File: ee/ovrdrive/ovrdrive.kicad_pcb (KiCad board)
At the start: 4 copper layers, 37.2 x 15 mm, 47 parts, among them J1 USB_A, Q1 Q_NMOS_DGS, U1 SM3257ENT, U2 FLASH, U3 ATtiny24A-MM, U4 74AUC1G32, U5 LMV321, U6 LM4040DBZ-2.5

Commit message: R0.1 released
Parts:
- JP1: moved to B.Cu
- moved JP1 4.10 mm to (129.4, 109.0), turned to 0 degrees
- moved JP2 1.91 mm to (138.1, 110.2)
- moved D2 0.10 mm to (139.6, 100.3)
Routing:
- net Net-(JP1-Pad2): track 5.93 -> 2.37 mm, vias 0 -> 1
- net +3.3V: track 40.1 -> 42.8 mm
- net Net-(JP2-Pad2): track 6.72 -> 8.53 mm
- net GND: vias 2 -> 13
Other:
- board text added: "OVRDRIVE Ryan Walker Interrupt Labs R0.1"

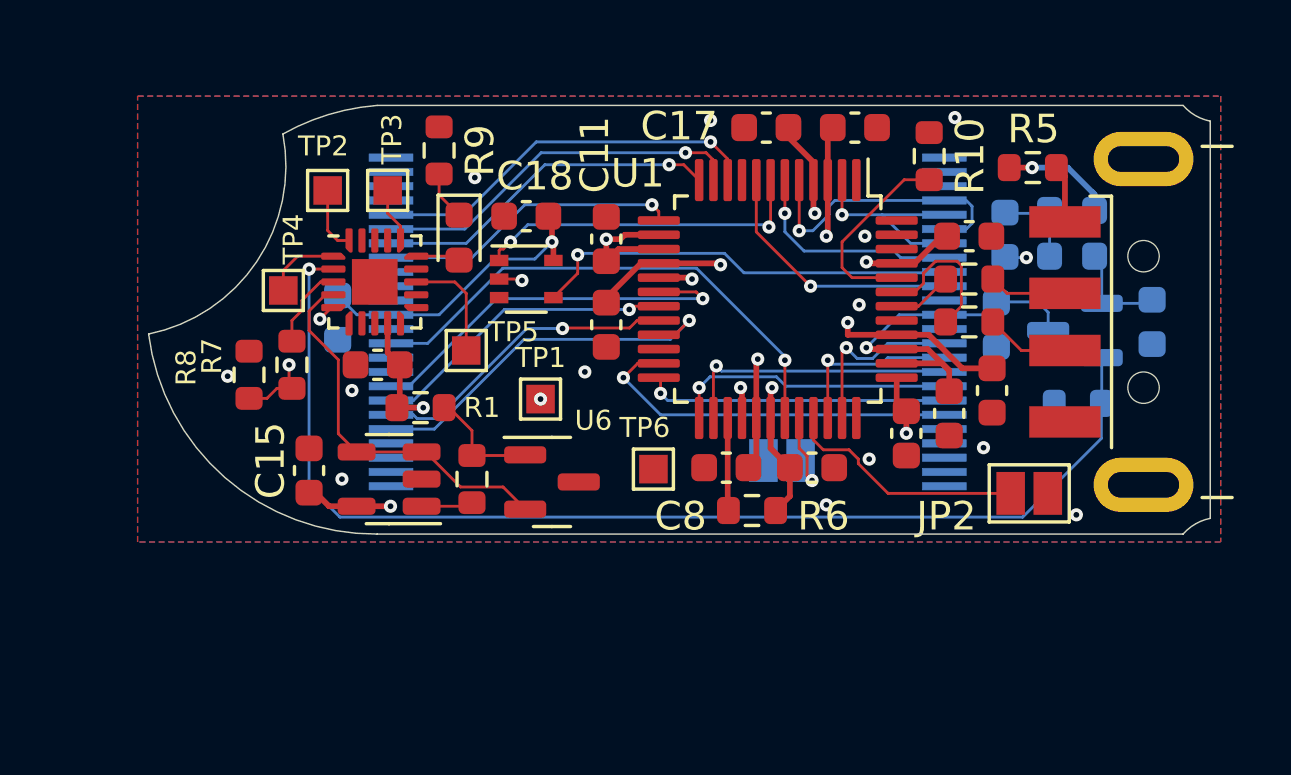
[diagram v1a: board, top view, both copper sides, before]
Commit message: Removed analog circuitry for spit detection, shortened entire board by 0.6mm to fit in enclosure.
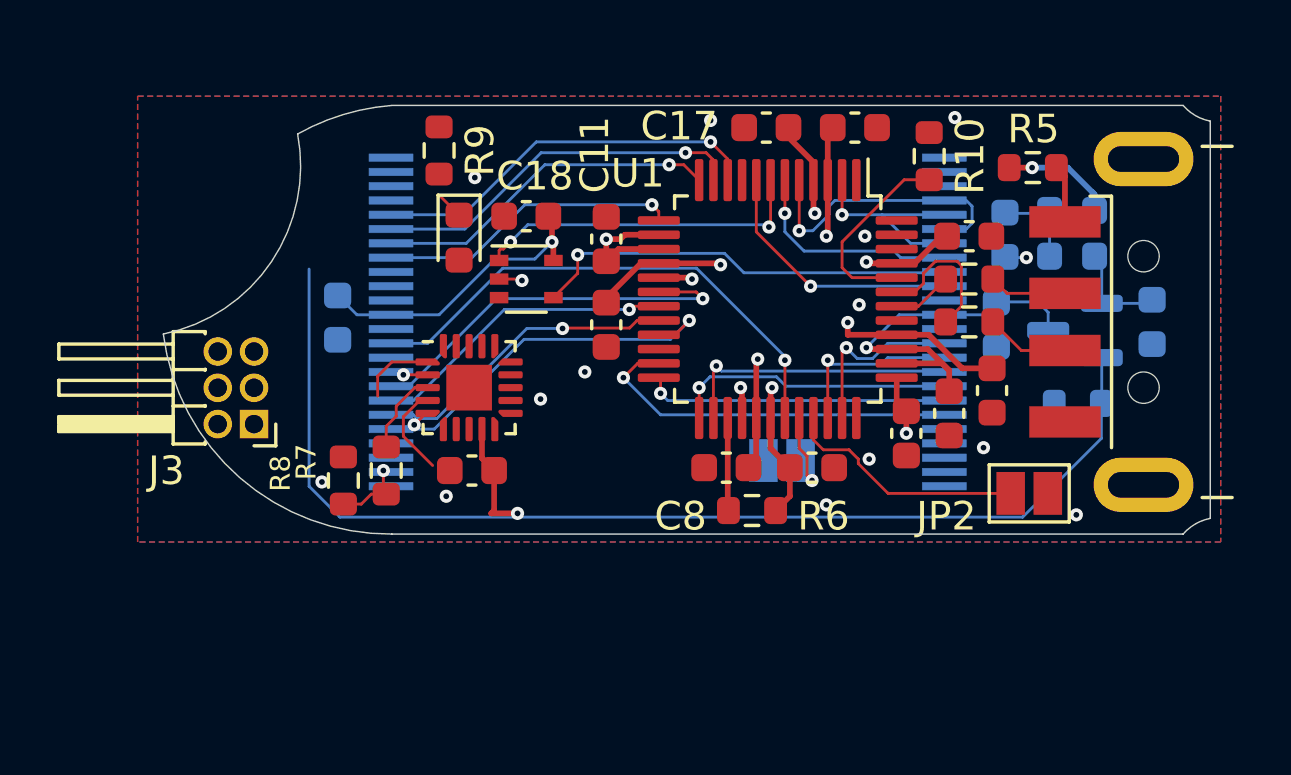
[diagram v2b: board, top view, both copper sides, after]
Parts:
- removed C15: 100nF, Capacitor_SMD:C_0603_1608Metric
- removed R1: 10k, Resistor_SMD:R_0603_1608Metric
- removed R2: 747k, Resistor_SMD:R_0603_1608Metric
- removed TP1, TP2, TP3, TP4, TP5, TP6: TestPoint, TestPoint:TestPoint_Pad_1.0x1.0mm
- removed U5: LMV321, Package_TO_SOT_SMD:SOT-23-5
- removed U6: LM4040DBZ-2.5, Package_TO_SOT_SMD:SOT-23
- added J3: Conn_02x03_Counter_Clockwise, Connector_PinHeader_1.27mm:PinHeader_2x03_P1.27mm_Horizontal, F.Cu at (111.0, 107.8)
- Q1: value Q_NMOS_DGS -> RU1J002YNTCL
- moved C4 4.96 mm to (118.6, 109.4)
- moved R7 4.96 mm to (115.6, 109.4)
- moved R8 4.96 mm to (114.1, 109.8)
- moved U3 4.96 mm to (118.5, 106.5)
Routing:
- net /Vs: track 13.4 -> 3.22 mm
- net Net-(R1-Pad2): track 4.05 -> 0.00 mm
- net /~{RST}: track 3.92 -> 0.00 mm
- net +5V: track 47.8 -> 44.7 mm, vias 5 -> 4
- net /MISO: track 2.29 -> 0.00 mm
- net /MOSI: track 1.94 -> 0.00 mm
- net Net-(J2-Pad2): track 1.81 -> 0.00 mm
- net Net-(D1-Pad2): track 1.56 -> 0.19 mm
- net Net-(D1-Pad1): track 1.73 -> 0.99 mm
- net GND: vias 13 -> 12
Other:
- board size 37.2 x 15 mm -> 36.6 x 15 mm

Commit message: Changes components and a leftover commit.
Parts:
- added C15: 22uF, Capacitor_SMD:C_0603_1608Metric, B.Cu at (139.6, 103.4)
- added D4: D_Schottky, Diode_SMD:D_0603_1608Metric, B.Cu at (113.9, 101.0)
- added Q2: SSM3J328R,LF, Package_TO_SOT_SMD:SOT-23, B.Cu at (139.3, 107.6)
- added Q3: RU1J002YNTCL, Package_TO_SOT_SMD:SOT-523, B.Cu at (142.5, 104.2)
- added R1: 1k, Resistor_SMD:R_0402_1005Metric, F.Cu at (115.1, 102.4)
- added R12: 1k, Resistor_SMD:R_0402_1005Metric, F.Cu at (123.1, 109.5)
- added R13: 1R, Resistor_SMD:R_0603_1608Metric, F.Cu at (116.9, 110.0)
- added R2: 10k, Resistor_SMD:R_0402_1005Metric, F.Cu at (114.8, 109.3)
- added TH1: 10k, Resistor_SMD:R_0603_1608Metric, F.Cu at (116.9, 108.5)
- added TP1: TestPoint, TestPoint:TestPoint_Pad_D1.0mm, F.Cu at (121.0, 105.7)
- added TP2: TestPoint, TestPoint:TestPoint_Pad_D1.0mm, F.Cu at (121.7, 103.1)
- C14: value 100nF -> 22uF
- D2, D3: value D -> D_Schottky
- Q1: value RU1J002YNTCL -> SSM3J328R,LF; moved to F.Cu
- R11: value 2.2R -> 1k; footprint Resistor_SMD:R_0603_1608Metric -> Resistor_SMD:R_0402_1005Metric
- R7, R8, R9: footprint Resistor_SMD:R_0603_1608Metric -> Resistor_SMD:R_0402_1005Metric
- moved Q1 19.8 mm to (120.6, 109.5)
- moved R8 5.35 mm to (113.9, 104.4)
- moved R7 5.05 mm to (114.9, 104.4)
- moved D1 2.93 mm to (117.5, 98.4)
- moved C14 2.89 mm to (139.6, 104.9), turned to 180 degrees
- moved C18 2.89 mm to (119.8, 97.7)
- moved U4 2.89 mm to (119.8, 99.9)
- moved C4 2.69 mm to (117.9, 106.8)
- moved U3 2.69 mm to (117.8, 103.9)
- moved R11 2.49 mm to (142.1, 108.0), turned to 180 degrees
- moved R9 1.56 mm to (115.9, 98.4), turned to 90 degrees
- moved J3 1.10 mm to (112.1, 107.8)
- turned C1 to 90 degrees
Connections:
- C1 pad 1: +3.3V -> Net-(D4-K)
- C14 pad 1: Net-(C14-Pad1) -> Net-(D3-K)
- C2 pad 1: +3.3V -> Net-(D4-K)
- D3 pad 1: Net-(C14-Pad1) -> Net-(D3-K)
- J3 pad 1: /MISO -> +5V
- J3 pad 6: +5V -> /MISO
- Q1 pad 1: Net-(C14-Pad1) -> /PB2
- Q1 pad 2: /KILL -> +5V
- Q1 pad 3: +3.3V -> Net-(Q1-D)
- R11 pad 1: GND -> Net-(Q2-G)
- R11 pad 2: /KILL -> Net-(D3-K)
- U2 pad 12: +3.3V -> Net-(D4-K)
- U2 pad 37: +3.3V -> Net-(D4-K)
- U3 pad 11: unconnected-(U3-Pad11) -> /PB0
- U3 pad 12: unconnected-(U3-Pad12) -> /PB1
- U3 pad 14: unconnected-(U3-Pad14) -> /PB2
- U3 pad 4: /Vs -> /PA1
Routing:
- net Net-(D4-K): track 0.00 -> 24.9 mm
- net /Distruct_PWM: track 41.3 -> 25.2 mm
- net /PB2: track 0.00 -> 15.0 mm, vias 0 -> 2
- net /~{RST}: track 0.00 -> 14.8 mm, vias 0 -> 1
- net /MOSI: track 0.00 -> 13.0 mm, vias 0 -> 1
- net /MISO: track 0.00 -> 8.84 mm
- net Net-(Q2-G): track 0.00 -> 8.58 mm
- net /PA1: track 0.00 -> 6.06 mm
- net +5V: track 44.7 -> 39.3 mm
- net Net-(D1-A): track 0.19 -> 5.34 mm
- net /SCK: track 2.66 -> 6.79 mm
- net +3.3V: track 42.8 -> 38.9 mm
- net /INHIBIT: track 13.8 -> 10.1 mm
- net Net-(C14-Pad1): track 3.57 -> 0.00 mm
- net /KILL: track 40.6 -> 37.2 mm, vias 1 -> 2
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- added copper zone on F.Cu, net +5V
- added copper zone on B.Cu, net Net-(D3-K)
- added copper zone on B.Cu, net Net-(D4-K)
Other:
- board text added: "OVRDRIVE Interrupt Labs R0.2"
- board text removed: "OVRDRIVE Ryan Walker Interrupt Labs R0.1"

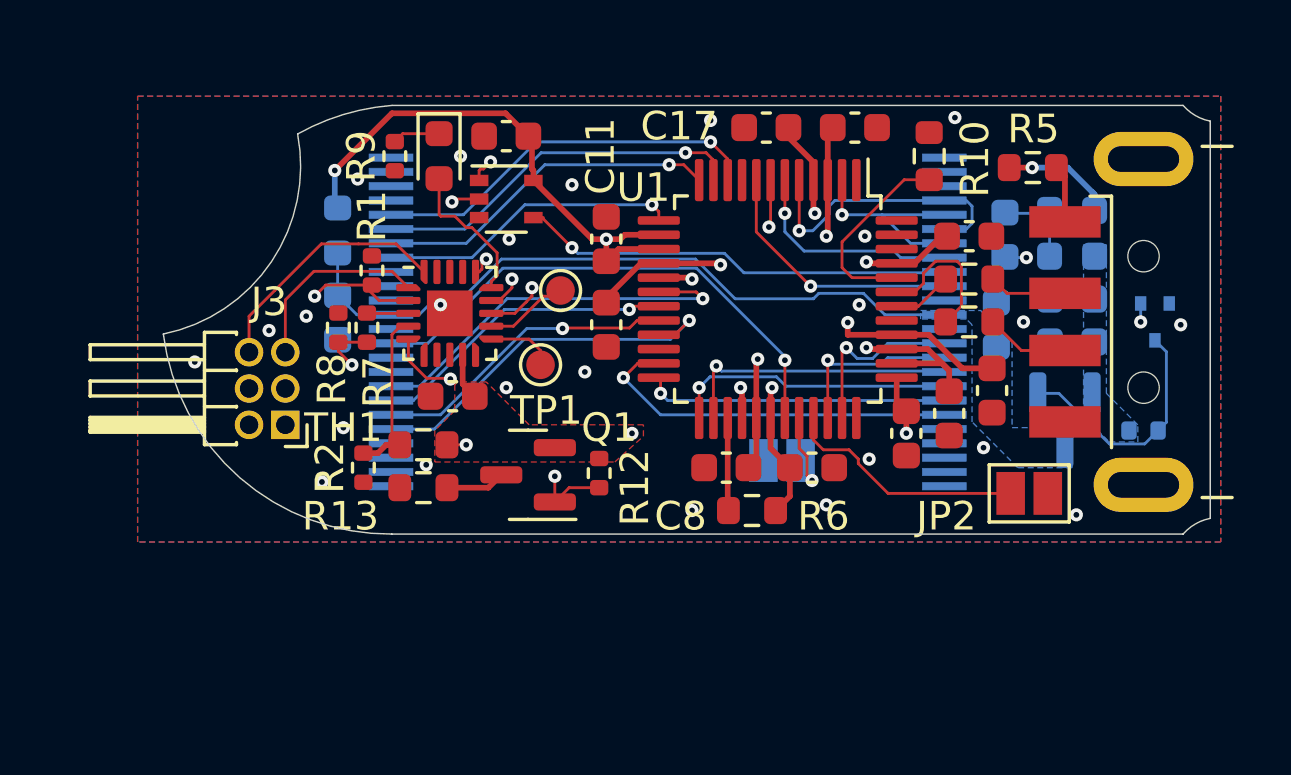
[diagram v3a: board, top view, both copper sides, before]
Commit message: Change the destruction circuit to an H-bridge.
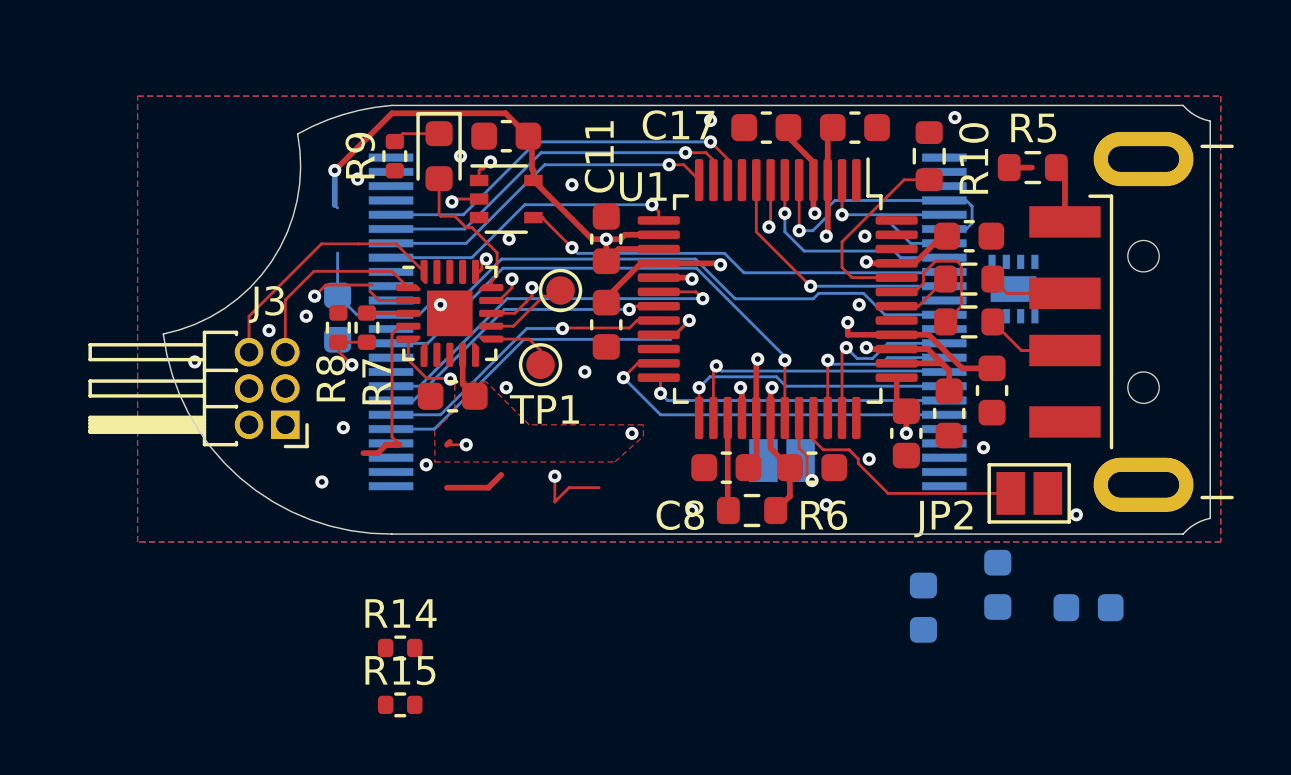
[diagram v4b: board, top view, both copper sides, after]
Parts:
- removed C15: 22uF, Capacitor_SMD:C_0603_1608Metric
- removed D2, D3, D4: D_Schottky, Diode_SMD:D_0603_1608Metric
- removed Q1, Q2: SSM3J328R,LF, Package_TO_SOT_SMD:SOT-23
- removed Q3: RU1J002YNTCL, Package_TO_SOT_SMD:SOT-523
- removed R1, R11, R12: 1k, Resistor_SMD:R_0402_1005Metric
- removed R13: 1R, Resistor_SMD:R_0603_1608Metric
- removed R2: 10k, Resistor_SMD:R_0402_1005Metric
- removed TH1: 10k, Resistor_SMD:R_0603_1608Metric
- added R14: 10k, Resistor_SMD:R_0402_1005Metric, F.Cu at (116.1, 115.6)
- added R15: 10k, Resistor_SMD:R_0402_1005Metric, F.Cu at (116.1, 117.6)
- added U5: DRV8837C, Package_SON:WSON-8-1EP_2x2mm_P0.5mm_EP0.9x1.6mm, B.Cu at (137.6, 103.0)
- C14: value 22uF -> 1uF
- C3: value 100nF -> 1uF
- U4: value 74AUC1G32 -> SN74LVC1G32DCKR
- moved C3 13.4 mm to (134.4, 114.2)
- moved C14 9.32 mm to (140.2, 114.2)
- moved C1 9.10 mm to (137.0, 113.4)
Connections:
- net Net-(D4-K) renamed VMEM
- C1 pad 2: GND -> VS
- C18 pad 2: GND -> VS
- C2 pad 2: GND -> VS
- C3 pad 2: /Distruct_PWM -> GND
- TP1 pad 1: /PB0 -> /PB1
- TP2 pad 1: /PB1 -> /PB2
- U2 pad 13: GND -> VS
- U2 pad 36: GND -> VS
- U3 pad 11: /PB0 -> /CHG2
- U3 pad 2: /KILL -> /CHG1
- U3 pad 4: /PA1 -> /IN2
- U3 pad 5: /Distruct_PWM -> /IN1
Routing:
- net /KILL: track 37.2 -> 0.00 mm, vias 2 -> 0
- net (no net): track 0.00 -> 37.2 mm, vias 0 -> 1
- net /Distruct_PWM: track 25.2 -> 0.00 mm, vias 2 -> 0
- net /IN1: track 0.00 -> 24.5 mm, vias 0 -> 1
- net Net-(Q2-G): track 8.58 -> 0.00 mm
- net /PA1: track 6.06 -> 0.00 mm
- net /IN2: track 0.00 -> 6.06 mm
- net +5V: track 39.3 -> 36.1 mm, vias 4 -> 3
- net Net-(D2-K): track 3.04 -> 0.00 mm
- net /PB1: track 2.94 -> 5.33 mm
- net /PB0: track 2.39 -> 0.00 mm
- net Net-(Q1-D): track 2.09 -> 0.00 mm
- net /CHG1: track 0.00 -> 1.48 mm
- net GND: track 0.04 -> 0.00 mm, vias 24 -> 22
- removed copper zone on B.Cu, net Net-(D3-K)
- removed copper zone on B.Cu, net VMEM

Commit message: Started the routing the new H-bridge.
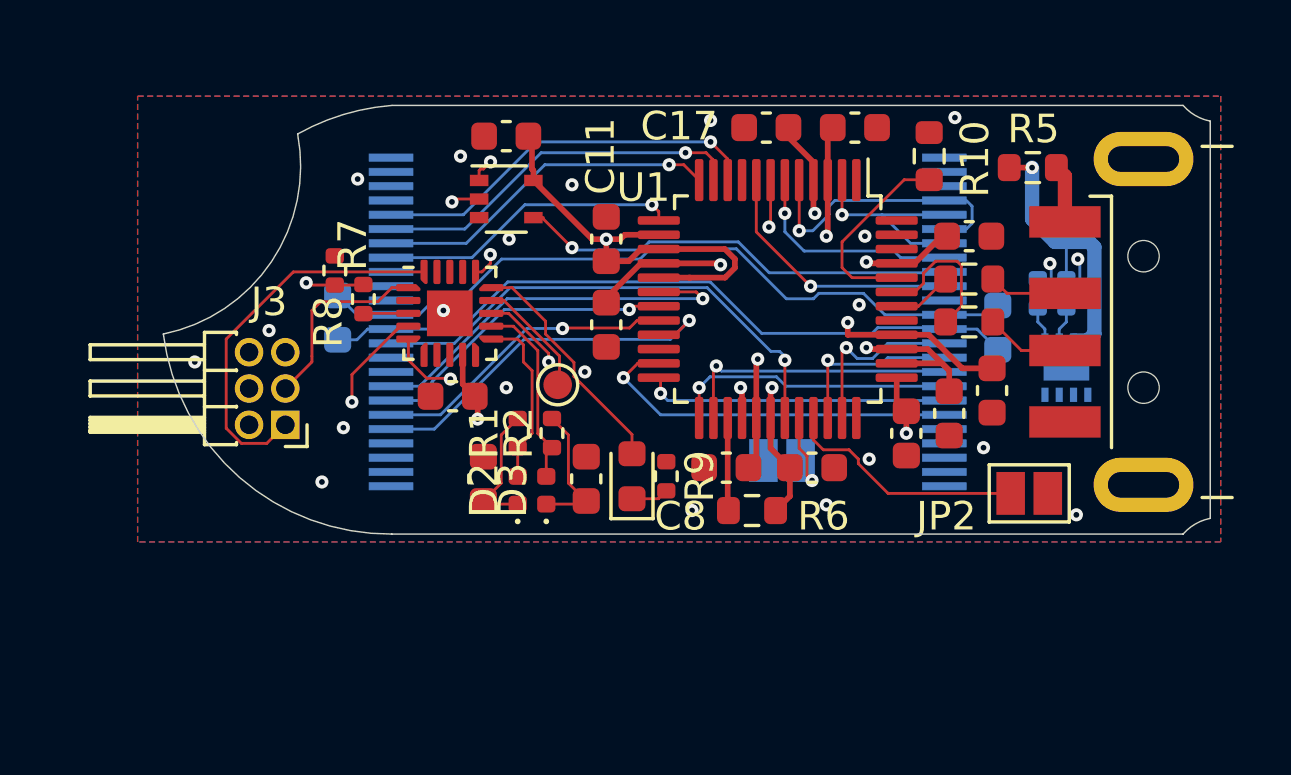
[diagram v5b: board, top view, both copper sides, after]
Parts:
- removed TP1: TestPoint, TestPoint:TestPoint_Pad_D1.0mm
- added D2: BAS70LP-7B, Diode_SMD:D_0402_1005Metric, F.Cu at (120.2, 110.1)
- added D3: BAS70LP-7B, Diode_SMD:D_0402_1005Metric, F.Cu at (121.2, 110.1)
- added R1: 1M, Resistor_SMD:R_0402_1005Metric, F.Cu at (120.2, 108.1)
- added R2: 1M, Resistor_SMD:R_0402_1005Metric, F.Cu at (121.4, 108.1)
- C14, C3: moved to F.Cu
- J3: value Conn_02x03_Counter_Clockwise -> AVR-ISP-6
- R14, R15: moved to B.Cu
- moved R15 26.6 mm to (138.4, 103.2), turned to -90 degrees
- moved R14 26.4 mm to (139.4, 103.2), turned to 90 degrees
- moved C14 18.1 mm to (122.6, 109.7), turned to 90 degrees
- moved C3 16.0 mm to (119.0, 109.7), turned to 90 degrees
- moved R9 14.7 mm to (125.4, 109.6), turned to -90 degrees
- moved D1 13.1 mm to (124.2, 109.6), turned to 90 degrees
- moved C1 9.00 mm to (137.0, 104.4), turned to -90 degrees
- moved U5 3.31 mm to (139.4, 105.8)
- moved TP2 3.30 mm to (121.6, 106.4)
- moved R8 2.00 mm to (113.8, 102.4)
- moved R7 1.01 mm to (114.8, 103.4), turned to -90 degrees
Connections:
- C18 pad 2: VS -> GND
- J3 pad 1: +5V -> /MISO
- J3 pad 2: /MOSI -> +5V
- J3 pad 3: /~{RST} -> /SCK
- J3 pad 4: GND -> /MOSI
- J3 pad 5: /SCK -> /~{RST}
- J3 pad 6: /MISO -> GND
- U3 pad 11: /CHG2 -> /CHG1
- U3 pad 12: /PB1 -> /CHG2
- U3 pad 2: /CHG1 -> unconnected-(U3-PA3-Pad2)
- U5 pad 7: Net-(JP3-A) -> +5V
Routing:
- net (no net): track 37.2 -> 0.00 mm, vias 1 -> 0
- net /IN2: track 6.06 -> 33.5 mm, vias 0 -> 2
- net VS: track 0.00 -> 25.1 mm
- net +5V: track 36.1 -> 51.8 mm
- net /PB2: track 15.0 -> 4.23 mm, vias 2 -> 0
- net /CHG2: track 0.00 -> 6.59 mm
- net /PB1: track 5.33 -> 0.00 mm
- net /IN1: track 24.5 -> 29.6 mm, vias 1 -> 2
- net /MISO: track 8.84 -> 13.6 mm
- net /CHG1: track 1.48 -> 6.15 mm
- net Net-(D2-K): track 0.00 -> 4.63 mm
- net Net-(D3-K): track 0.00 -> 4.63 mm
- net +3.3V: track 38.9 -> 34.3 mm, vias 8 -> 6
- net Net-(D1-A): track 5.34 -> 8.28 mm
- net /~{RST}: track 14.8 -> 13.4 mm
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- removed copper zone on F.Cu, net +5V

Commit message: R0.3 released
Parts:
- added C15: 100nF, Capacitor_SMD:C_0603_1608Metric, B.Cu at (142.4, 108.0)
- added C16: 100nF, Capacitor_SMD:C_0603_1608Metric, B.Cu at (141.7, 103.4)
- R14, R15: footprint Resistor_SMD:R_0402_1005Metric -> Resistor_SMD:R_0603_1608Metric
- moved R14 2.12 mm to (139.7, 101.1)
- moved R15 2.04 mm to (138.0, 101.2)
- moved R9 0.10 mm to (125.5, 109.6)
- moved C14 0.09 mm to (122.6, 109.6)
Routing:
- net VS: track 25.1 -> 40.3 mm
- net VMEM: track 25.6 -> 36.7 mm, vias 0 -> 2
- net +3.3V: track 34.3 -> 42.5 mm, vias 6 -> 7
- net /IN1: track 29.6 -> 31.0 mm
- net +5V: track 51.8 -> 52.7 mm
- net GND: vias 20 -> 27
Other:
- board text added: "OVRDRIVE Interrupt Labs R0.3"
- board text removed: "OVRDRIVE Interrupt Labs R0.2"
